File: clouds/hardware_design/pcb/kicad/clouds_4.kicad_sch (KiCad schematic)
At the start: 31 parts

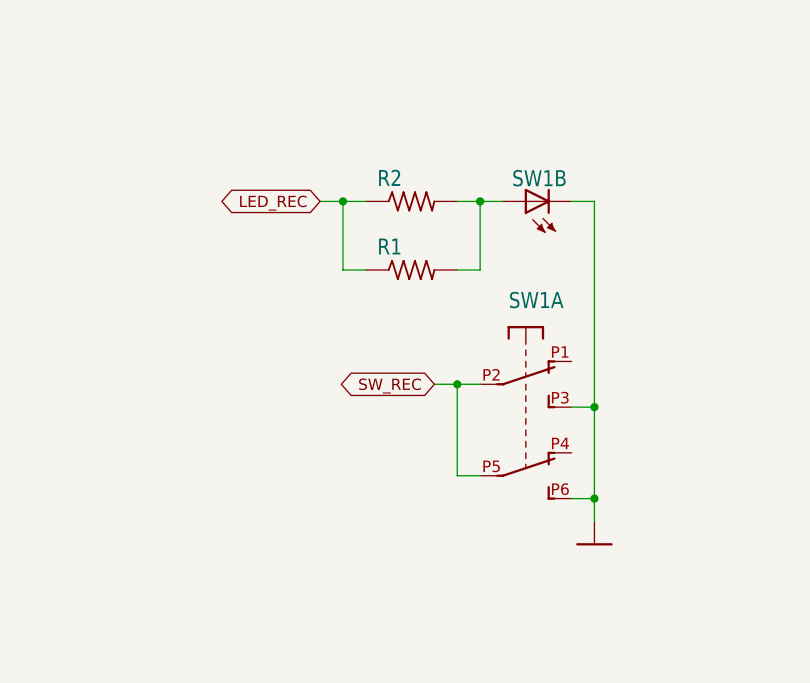
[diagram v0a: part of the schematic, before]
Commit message: clouds new kind of LED/switch pushbutton
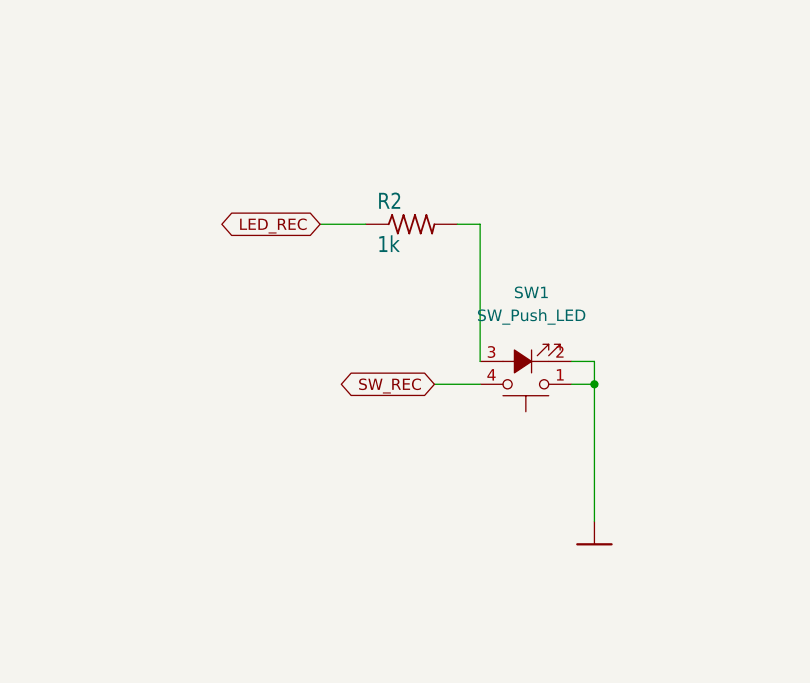
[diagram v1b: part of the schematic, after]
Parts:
- removed R1: (no value), symbol clouds-eagle-import:R-US_R0603
- removed SW1: (no value), symbol clouds-eagle-import:LP4OA1PBCT
- added SW1: SW_Push_LED, Supercell 1.3:C&K_D6R, symbol Switch:SW_Push_LED
- R2: value (none) -> 1k
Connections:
- net GND: now also SW1.1, SW1.2
- net SW_REC: now also SW1.4
- net at R2.2: now also SW1.3
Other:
- moved on the sheet: R2
